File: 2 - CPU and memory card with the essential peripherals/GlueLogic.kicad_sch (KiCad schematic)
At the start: 13 parts, among them J12 INT SRC, SW3 CONFIG, U20 ATF22V10C, U21 ATF22V10C, U22 ATF22V10C, U23 ATF22V10C, U24 74HCT574, U25 74HCT573, U7 74HCT574

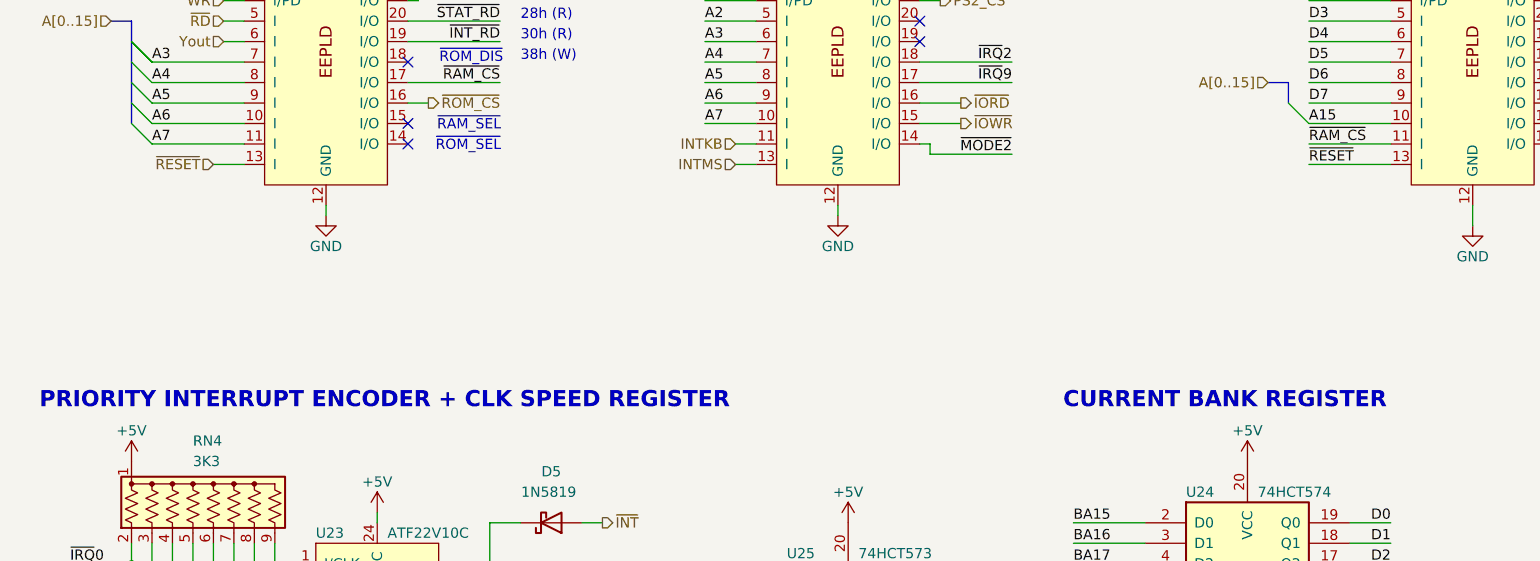
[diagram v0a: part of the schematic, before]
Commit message: Added existing assembler code and PLD files
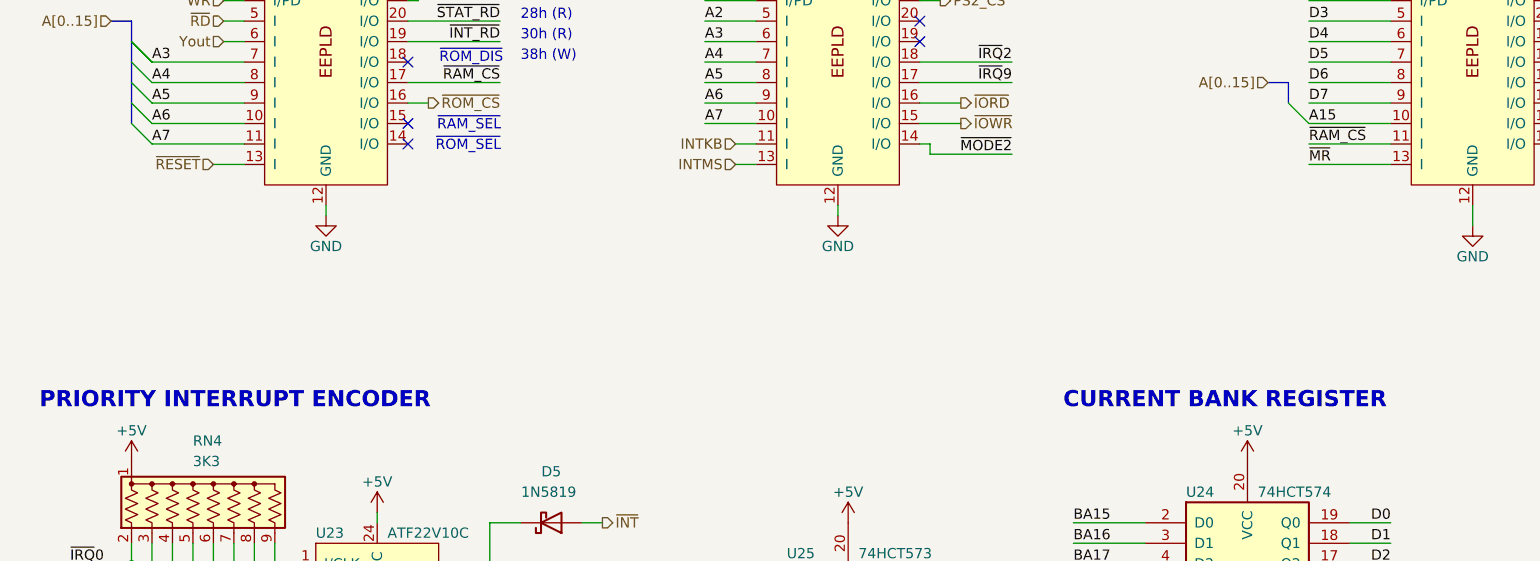
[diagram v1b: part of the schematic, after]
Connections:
- net ~{RESET}: no longer U22.13 (I)
- new net ~{MR}: U22.13 (I)
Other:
- note added: "PRIORITY INTERRUPT ENCODER"
- note removed: "PRIORITY INTERRUPT ENCODER + CLK SPEED REGISTER"
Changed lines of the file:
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@@
     (effects (font (size 2 2) (thickness 0.508) bold) (justify left bottom))
   )
-  (text "PRIORITY INTERRUPT ENCODER + CLK SPEED REGISTER" (at 19.05 93.98 0)
+  (text "PRIORITY INTERRUPT ENCODER" (at 19.05 93.98 0)
     (effects (font (size 2 2) (thickness 0.508) bold) (justify left bottom))
   )
@@
     (effects (font (size 1.27 1.27)) (justify left bottom))
   )
-  (label "~{RESET}" (at 176.53 63.5 0) (fields_autoplaced)
-    (effects (font (size 1.27 1.27)) (justify left bottom))
-  )
+  (label "~{MR}" (at 176.53 63.5 0) (fields_autoplaced)
+    (effects (font (size 1.27 1.27)) (justify left bottom))
+  )
